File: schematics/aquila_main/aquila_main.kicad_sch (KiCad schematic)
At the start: 40 parts, among them IC1 TPS62152, IC2 TPS62132

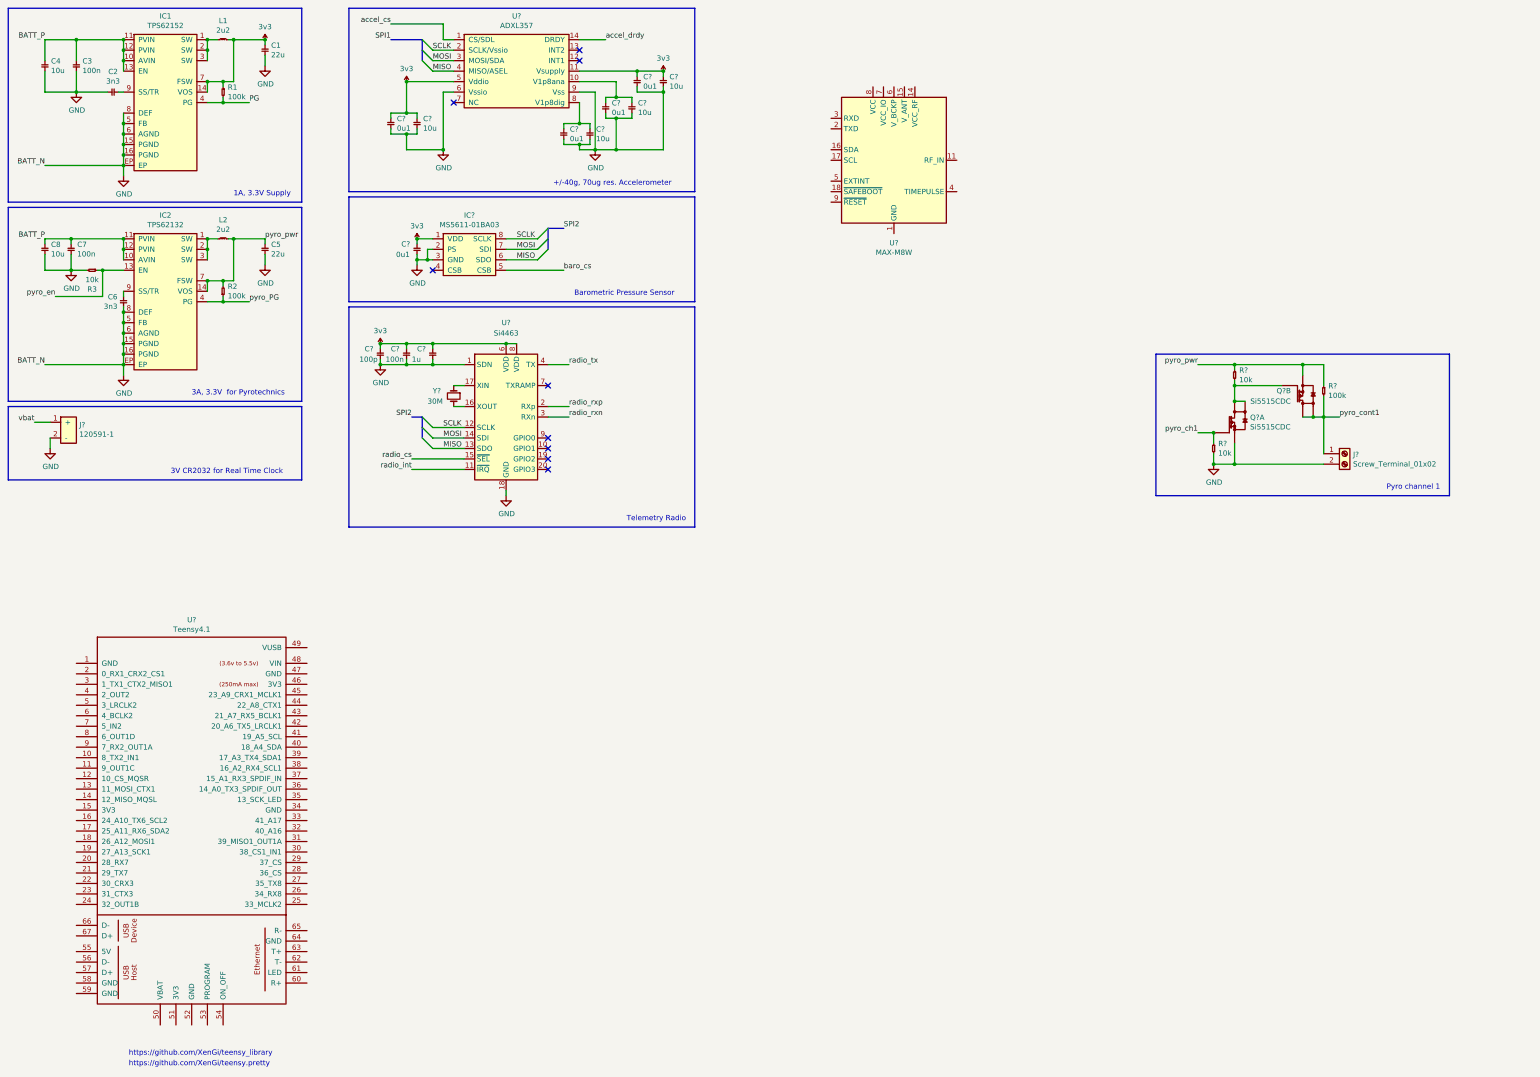
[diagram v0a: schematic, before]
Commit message: added connections for GPS
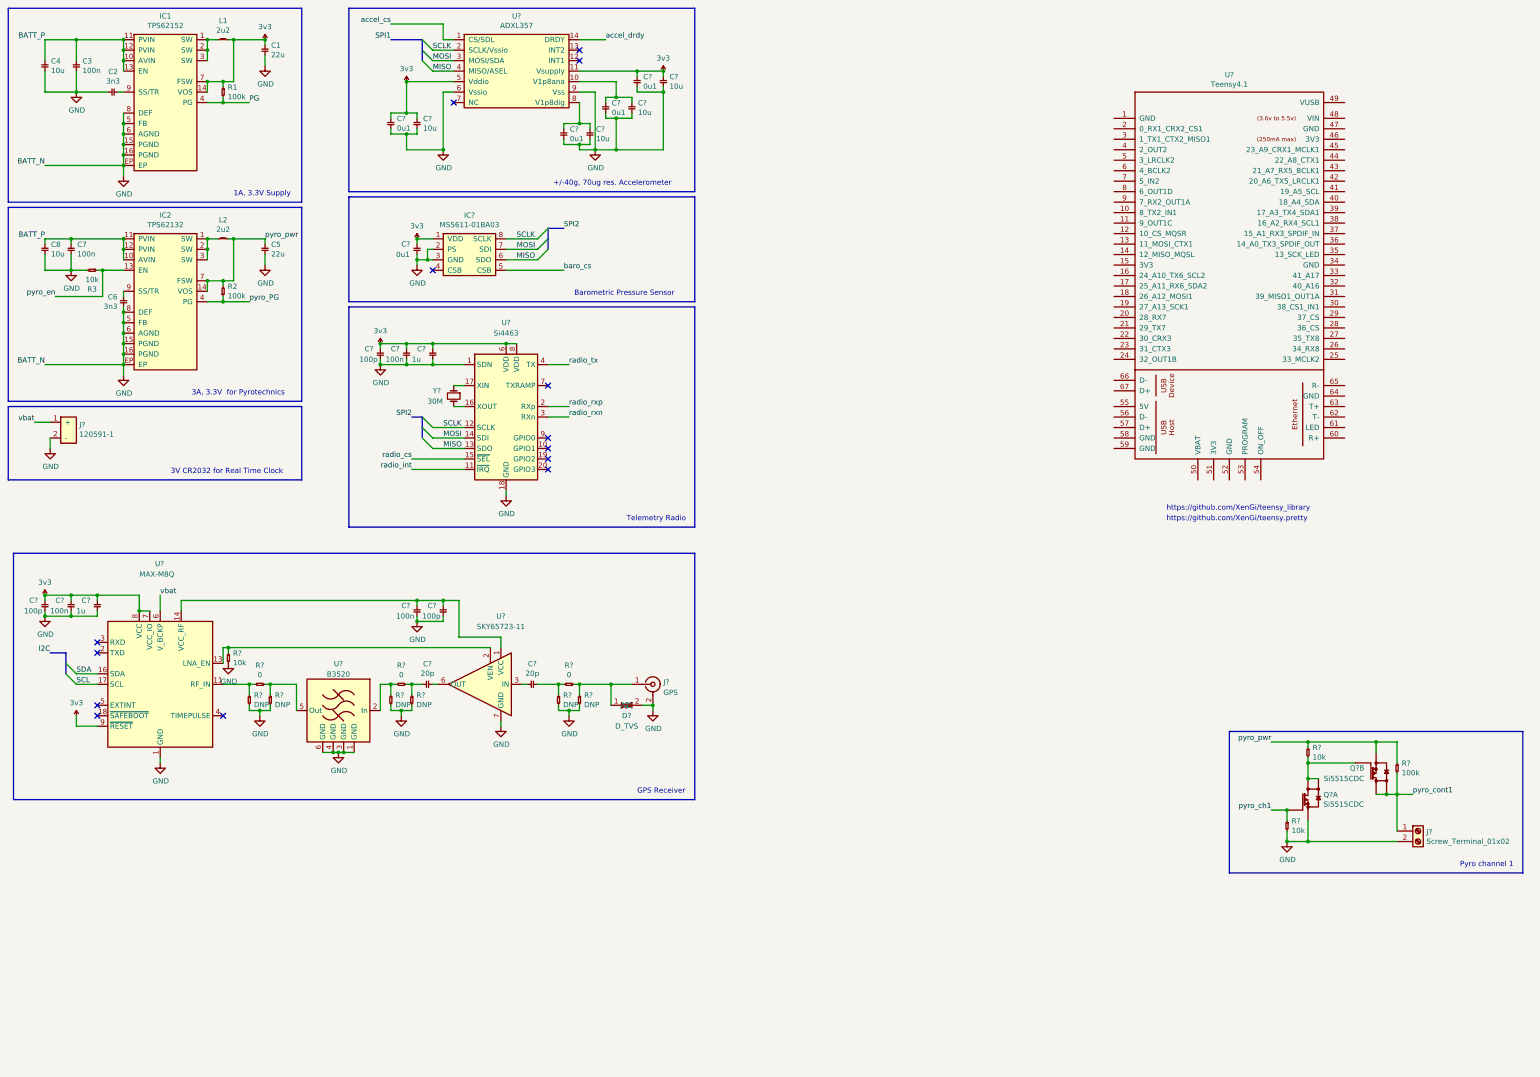
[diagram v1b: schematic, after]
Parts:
- removed U?: MAX-M8W, RF_GPS:ublox_MAX, symbol RF_GPS:MAX-M8W
- added C? (x2): 100p, symbol aquila_main-rescue:C-cusf-kicad
- added C? (x2): 20p, symbol aquila_main-rescue:C-cusf-kicad
- added C? (x2): 100n, symbol aquila_main-rescue:C-cusf-kicad
- added C?: 1u, symbol aquila_main-rescue:C-cusf-kicad
- added D?: D_TVS, symbol aquila:D_TVS
- added J?: GPS, symbol Connector:Conn_Coaxial
- added R? (x6): DNP, symbol aquila_main-rescue:R-cusf-kicad
- added R? (x3): 0, symbol aquila_main-rescue:R-cusf-kicad
- added R?: 10k, symbol aquila_main-rescue:R-cusf-kicad
- added U?: B3520, symbol aquila:B3520
- added U?: SKY65723-11, symbol aquila:SKY65723-11
- added U?: MAX-M8Q, RF_GPS:ublox_MAX, symbol RF_GPS:MAX-M8Q
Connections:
- net 3v3: now also C?.1, C?.1, C?.1, U?.7 (VCC_IO), U?.8 (VCC), U?.9 (~{RESET})
- net GND: now also C?.2, C?.2, C?.2, C?.2, C?.2, D?.2 (A2), J?.2 (Ext), R?.2, R?.2, R?.2, R?.2, R?.2, R?.2, R?.2, U?.1 (GND), U?.1 (GND), U?.10 (GND), U?.12 (GND), U?.3 (GND), U?.4 (GND), U?.6 (GND), U?.7 (GND)
- net vbat: now also U?.6 (V_BCKP)
- new net: C?.1, U?.3 (IN)
- new net: C?.2, R?.1, R?.2
- new net: R?.1, R?.2, U?.11 (RF_IN)
- new net: D?.1 (A1), J?.1 (In), R?.1, R?.1
- new net: C?.1, C?.1, U?.1 (VCC), U?.14 (VCC_RF)
- new net: R?.1, R?.2, U?.2 (In)
- new net: C?.1, R?.1, R?.1
- new net: R?.1, R?.1, U?.5 (Out)
- new net: R?.1, U?.13 (LNA_EN), U?.2 (VEN)
- new net: C?.2, U?.6 (OUT)
- new net SCL: U?.17 (SCL)
- new net SDA: U?.16 (SDA)
- no-connect marks 9 -> 14
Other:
- note added: "GPS Receiver"
- moved on the sheet: J?, Q?A, Q?B, R?, U?

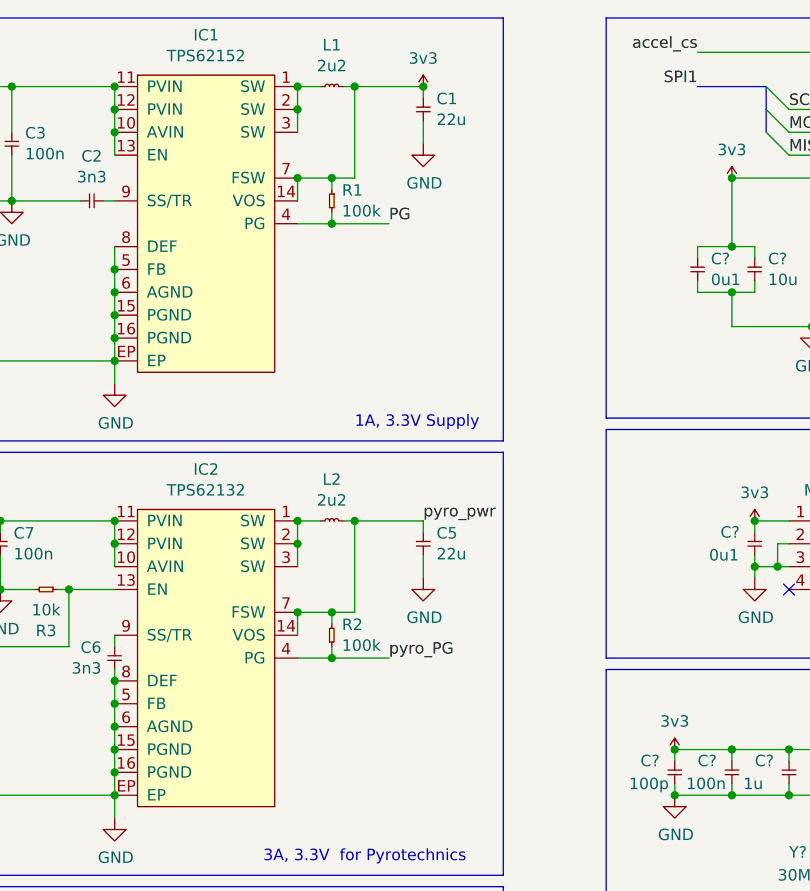
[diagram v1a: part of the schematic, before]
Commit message: added power indicator LEDs
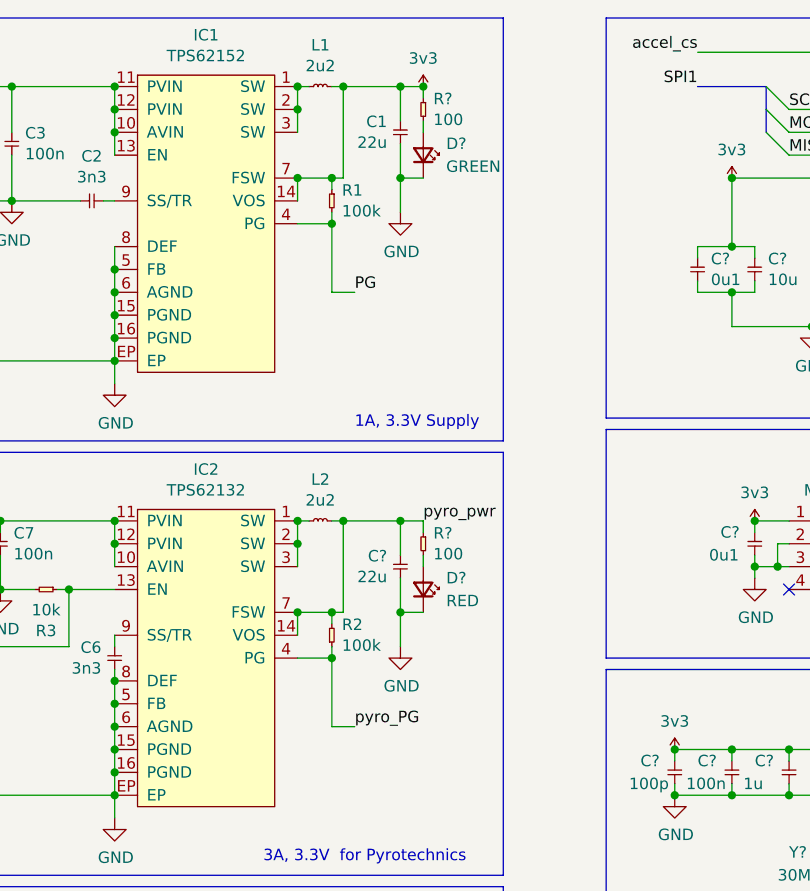
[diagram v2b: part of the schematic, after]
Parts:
- removed C5: 22u, symbol aquila_main-rescue:C-cusf-kicad
- added C?: 22u, symbol aquila_main-rescue:C-cusf-kicad
- added D?: RED, symbol Device:LED_Small
- added D?: GREEN, symbol Device:LED_Small
- added R? (x2): 100, symbol aquila_main-rescue:R-cusf-kicad
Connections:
- net 3v3: now also R?.1
- net GND: now also C?.2, D?.1 (K), D?.1 (K)
- net pyro_pwr: now also C?.1, R?.1
- new net: D?.2 (A), R?.2 (x2)
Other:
- moved on the sheet: C1, L1, L2

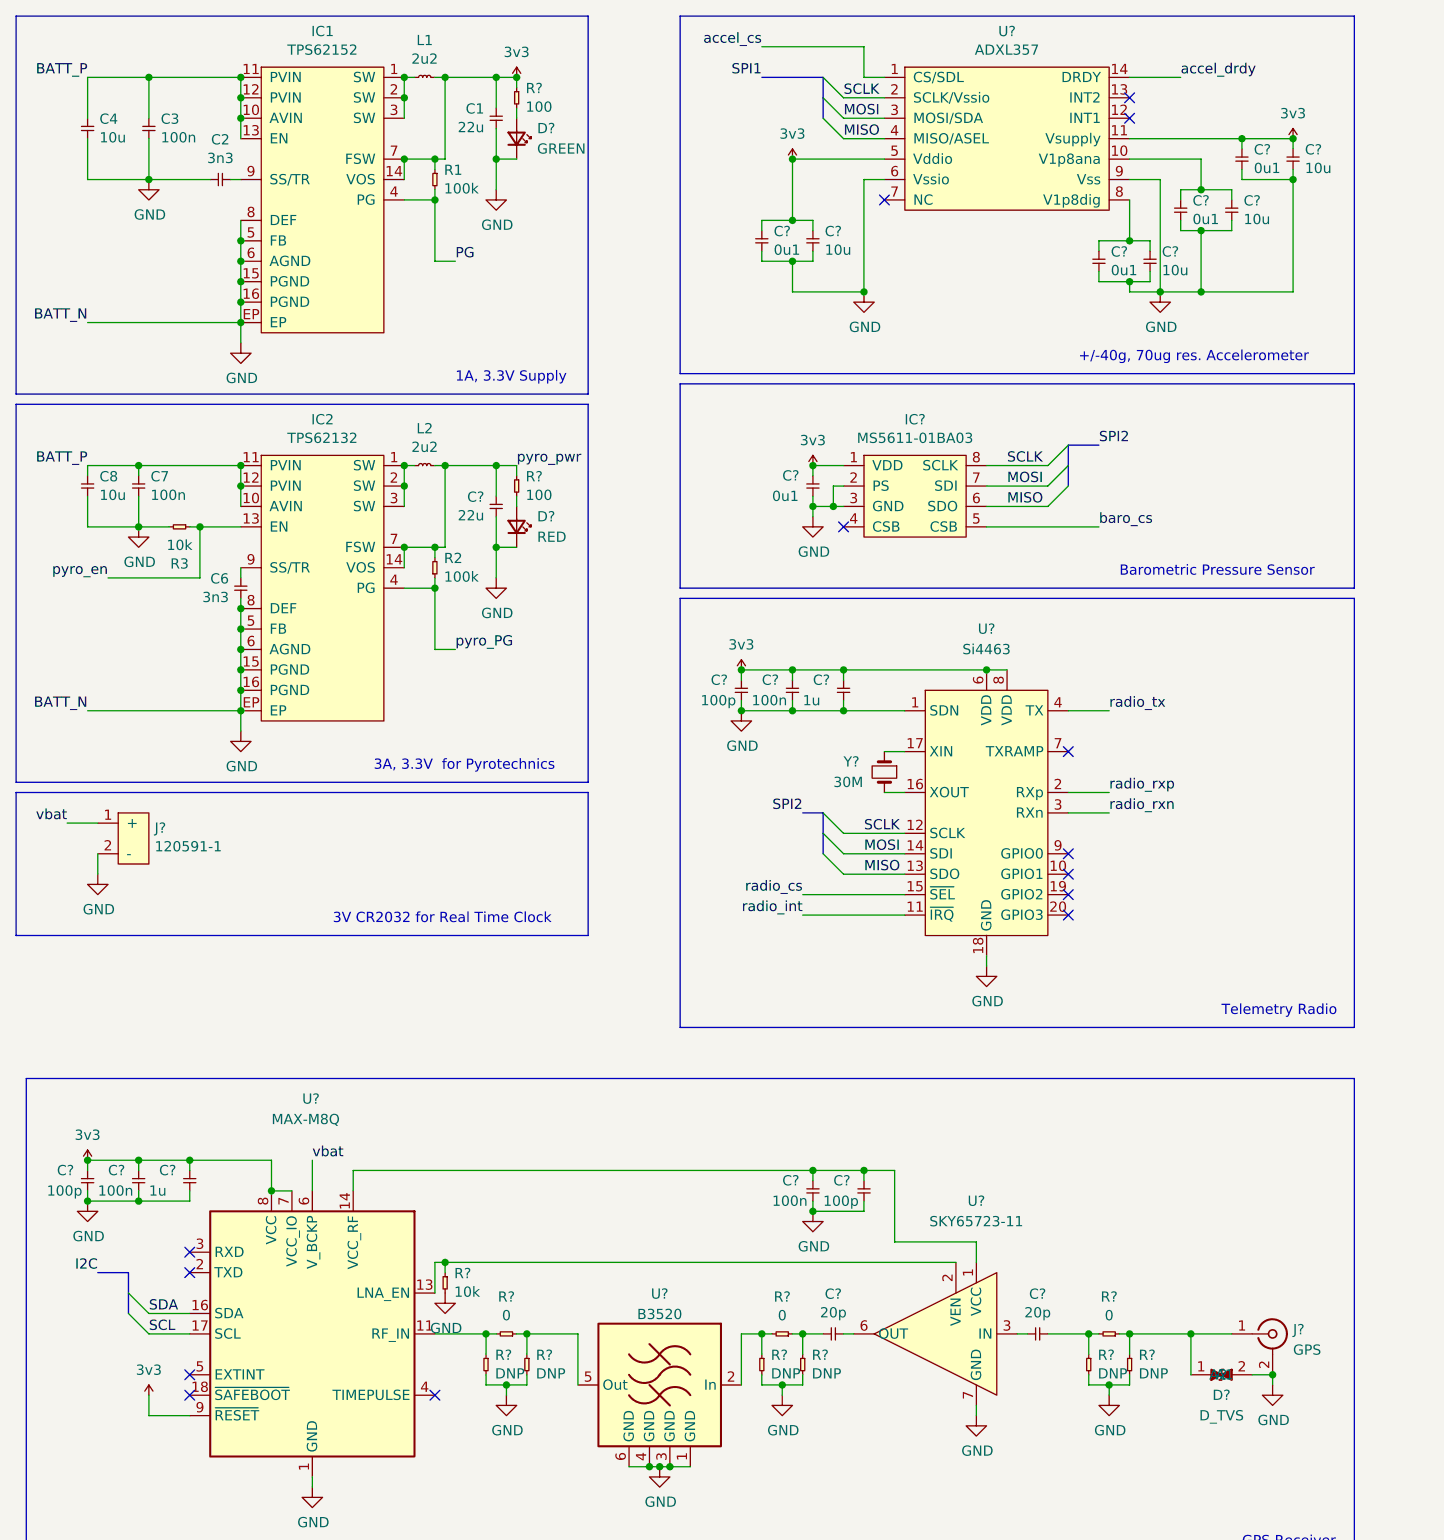
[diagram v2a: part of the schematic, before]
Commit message: removed dependence on deprecated symbol library
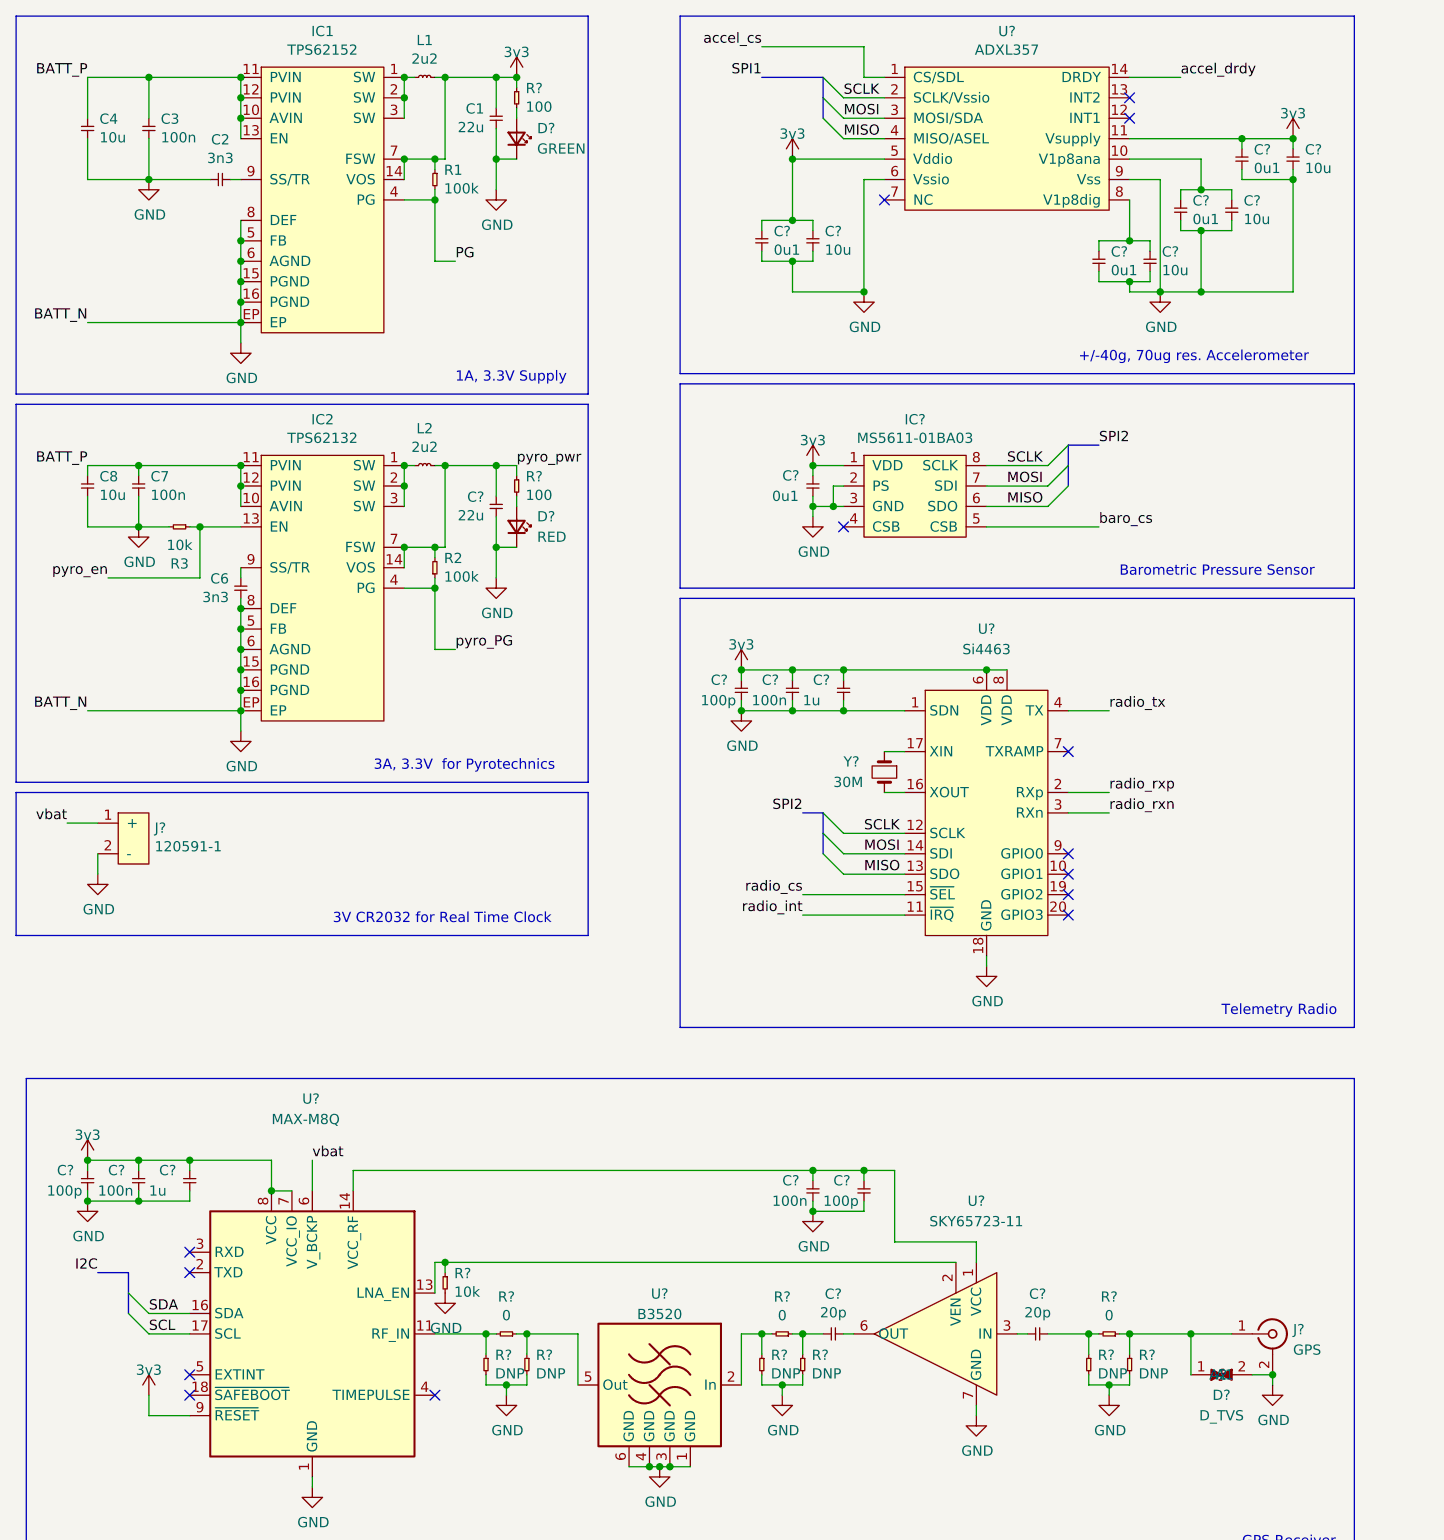
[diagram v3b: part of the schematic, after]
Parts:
- C1, C2, C3, C4, C6, C7, C8, C? (x20): symbol aquila_main-rescue:C-cusf-kicad -> aquila:C-cusf-kicad
- IC1, IC2: symbol aquila_main-rescue:TPS62132-cusf-kicad -> aquila:TPS62132
- IC?: symbol cusf-kicad:MS5611-01BA03 -> aquila:MS5611-01BA03
- L1, L2: symbol aquila_main-rescue:L-cusf-kicad -> aquila:L-cusf-kicad
- Q? (x2): symbol aquila_main-rescue:Si5515CDC-cusf-kicad -> aquila:Si5515CDC-cusf-kicad
- R1, R2, R3, R? (x15): symbol aquila_main-rescue:R-cusf-kicad -> aquila:R-cusf-kicad
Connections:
- net 3v3 renamed +3V3
